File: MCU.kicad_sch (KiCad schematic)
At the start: 22 parts, among them J10 TIM3_OUT_CONN, J11 Conn_01x05_Pin, J12 Conn_01x04_Pin, J13 GPIO_OUT_CONN, J8 Conn_01x08_Pin, Y1 ABM3-8.000MHZ-D2Y-T

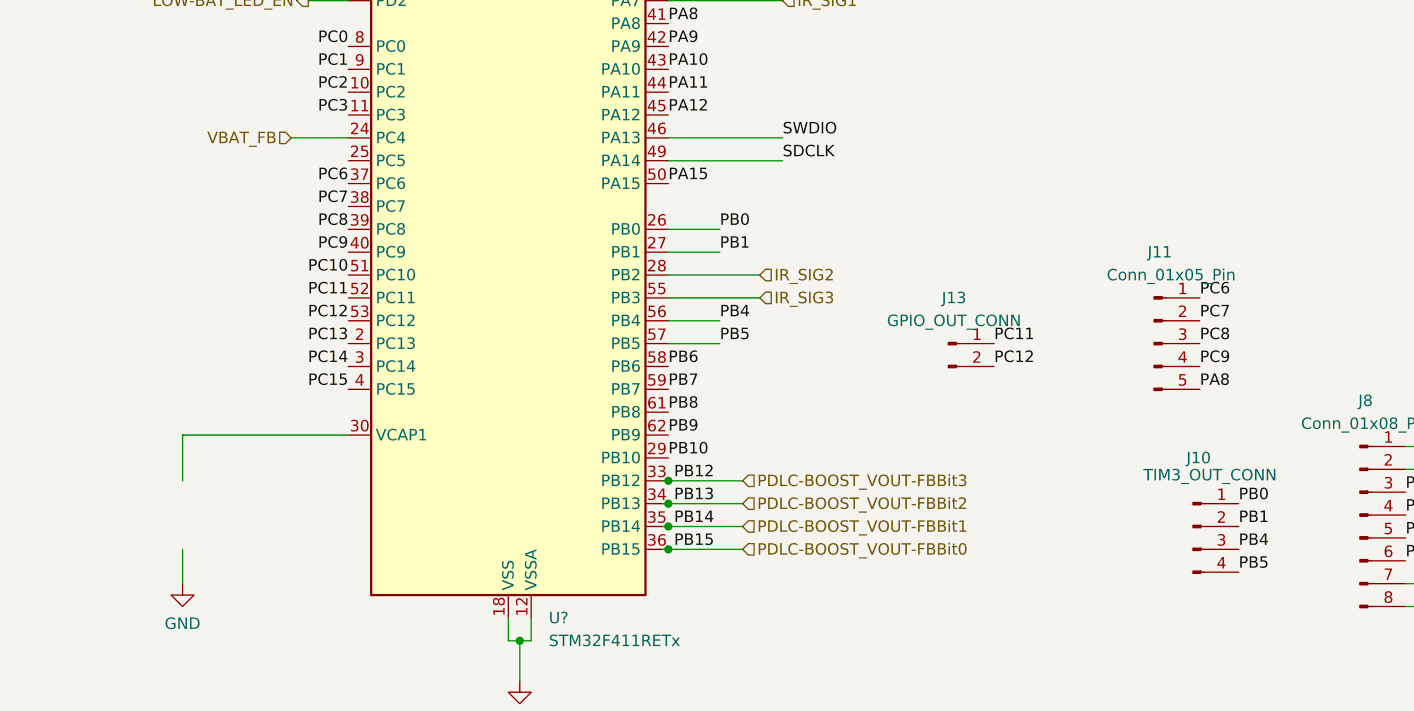
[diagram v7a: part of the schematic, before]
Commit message: PCBv2.02
Toepassingen van wouters feedback.
Condensatoren beter geplaatst bij pdlc, mosfet toegevoegd bij fb bat, extra vias toegevoegd en traces verschoven voor betere GND plane connecties
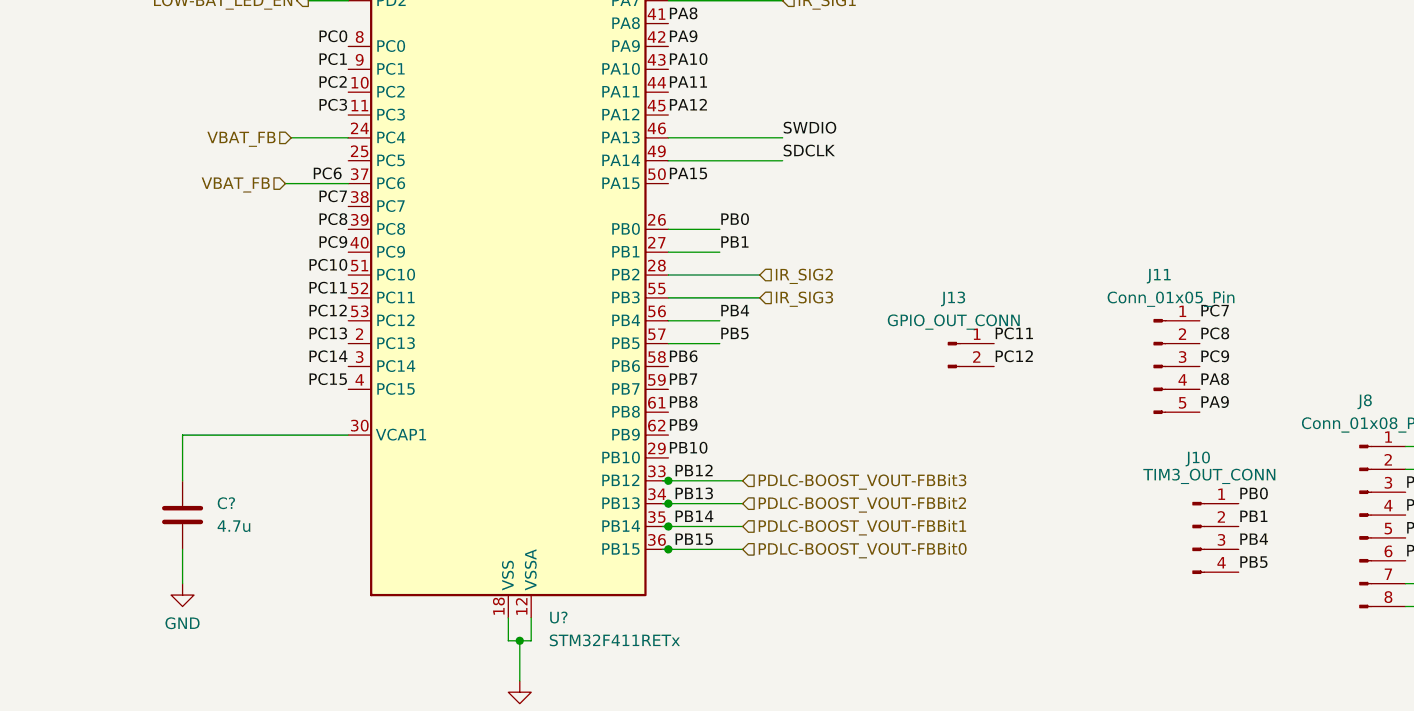
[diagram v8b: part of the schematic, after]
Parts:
- added C?: 4.7u, Capacitor_SMD:C_0805_2012Metric_Pad1.18x1.45mm_HandSolder, symbol Device:C
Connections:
- net GND: now also C?.2
- net PA8: now also J11.4 (Pin_4); no longer J11.5 (Pin_5)
- net PA9: now also J11.5 (Pin_5)
- net PC7: now also J11.1 (Pin_1); no longer J11.2 (Pin_2)
- net PC8: now also J11.2 (Pin_2); no longer J11.3 (Pin_3)
- net PC9: now also J11.3 (Pin_3); no longer J11.4 (Pin_4)
- net VBAT_FB: now also U?.37 (PC6)
- net at U?.30 (VCAP1): now also C?.1
- removed net PC6: J11.1 (Pin_1), U?.37 (PC6)
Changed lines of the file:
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@@
+    (stroke (width 0) (type default))
+  )
+  (wire (pts (xy 119.38 93.98) (xy 126.365 93.98))
     (stroke (width 0) (type default))
   )
@@
     (effects (font (size 1.27 1.27)) (justify left bottom))
   )
-  (label "PC6" (at 220.98 106.68 0) (fields_autoplaced)
-    (effects (font (size 1.27 1.27)) (justify left bottom))
-  )
   (label "PB0" (at 167.64 99.06 0) (fields_autoplaced)
     (effects (font (size 1.27 1.27)) (justify left bottom))
@@
     (effects (font (size 1.27 1.27)) (justify left bottom))
   )
-  (label "PC6" (at 126.365 93.98 180) (fields_autoplaced)
+  (label "PC6" (at 125.73 93.98 180) (fields_autoplaced)
     (effects (font (size 1.27 1.27)) (justify right bottom))
   )
@@
   )
   (label "PB13" (at 162.56 129.54 0) (fields_autoplaced)
+    (effects (font (size 1.27 1.27)) (justify left bottom))
+  )
+  (label "PA9" (at 220.98 119.38 0) (fields_autoplaced)
     (effects (font (size 1.27 1.27)) (justify left bottom))
   )
@@
   (hierarchical_label "H-BRIDGE_IN_B" (shape output) (at 174.752 58.42 0) (fields_autoplaced)
     (effects (font (size 1.27 1.27)) (justify left))
+  )
+  (hierarchical_label "VBAT_FB" (shape input) (at 119.38 93.98 180) (fields_autoplaced)
+    (effects (font (size 1.27 1.27)) (justify right))
   )
   (symbol (lib_id "power:GND") (at 251.46 125.73 0) (unit 1)
@@
     )
   )
+  (symbol (lib_id "Device:C") (at 107.95 130.81 0) (unit 1)
+    (in_bom yes) (on_board yes) (dnp no) (fields_autoplaced)
+    (property "Reference" "C?" (at 111.76 129.54 0)
+      (effects (font (size 1.27 1.27)) (justify left))
+    )
+    (property "Value" "4.7u" (at 111.76 132.08 0)
+      (effects (font (size 1.27 1.27)) (justify left))
+    )
+    (property "Footprint" "Capacitor_SMD:C_0805_2012Metric_Pad1.18x1.45mm_HandSolder" (at 108.9152 134.62 0)
+      (effects (font (size 1.27 1.27)) hide)
+    )
+    (property "Datasheet" "~" (at 107.95 130.81 0)
+      (effects (font (size 1.27 1.27)) hide)
+    )
+    (pin "1")
+    (pin "2")
+    (instances
+      (project "RookBril"
+        (path "/5dc439a9-720d-4bdc-b61f-78a76fde4df5"
+          (reference "C?") (unit 1)
+        )
+        (path "/5dc439a9-720d-4bdc-b61f-78a76fde4df5/d4272076-6289-417e-a51e-9430beab01b7"
+          (reference "C29") (unit 1)
+        )
+      )
+    )
+  )
   (symbol (lib_id "Connector:Conn_01x03_Pin") (at 27.94 60.96 0) (unit 1)
     (in_bom yes) (on_board yes) (dnp no)
@@
     )
   )
-  (symbol (lib_id "power:+3V0") (at 251.46 138.43 0) (unit 1)
-    (in_bom yes) (on_board yes) (dnp no) (fields_autoplaced)
-    (property "Reference" "#PWR?" (at 251.46 142.24 0)
-      (effects (font (size 1.27 1.27)) hide)
-    )
-    (property "Value" "+3V0" (at 251.46 134.62 0)
-      (effects (font (size 1.27 1.27)))
-    )
-    (property "Footprint" "" (at 251.46 138.43 0)
-      (effects (font (size 1.27 1.27)) hide)
-    )
-    (property "Datasheet" "" (at 251.46 138.43 0)
-      (effects (font (size 1.27 1.27)) hide)
-    )
-    (pin "1")
-    (instances
-      (project "RookBril"
-        (path "/5dc439a9-720d-4bdc-b61f-78a76fde4df5"
-          (reference "#PWR?") (unit 1)
-        )
-        (path "/5dc439a9-720d-4bdc-b61f-78a76fde4df5/d4272076-6289-417e-a51e-9430beab01b7"
-          (reference "#PWR070") (unit 1)
-        )
-      )
-    )
-  )
-  (symbol (lib_id "power:+3V0") (at 98.425 17.78 0) (unit 1)
-    (in_bom yes) (on_board yes) (dnp no) (fields_autoplaced)
-    (property "Reference" "#PWR?" (at 98.425 21.59 0)
-      (effects (font (size 1.27 1.27)) hide)
-    )
-    (property "Value" "+3V0" (at 98.425 13.97 0)
-      (effects (font (size 1.27 1.27)))
-    )
-    (property "Footprint" "" (at 98.425 17.78 0)
-      (effects (font (size 1.27 1.27)) hide)
-    )
-    (property "Datasheet" "" (at 98.425 17.78 0)
-      (effects (font (size 1.27 1.27)) hide)
-    )
-    (pin "1")
-    (instances
-      (project "RookBril"
-        (path "/5dc439a9-720d-4bdc-b61f-78a76fde4df5"
-          (reference "#PWR?") (unit 1)
-        )
-        (path "/5dc439a9-720d-4bdc-b61f-78a76fde4df5/d4272076-6289-417e-a51e-9430beab01b7"
-          (reference "#PWR030") (unit 1)
-        )
-      )
-    )
-  )
-  (symbol (lib_id "Connector:Conn_01x05_Pin") (at 215.9 111.76 0) (unit 1)
+  (symbol (lib_id "Connector:Conn_01x05_Pin") (at 215.9 114.3 0) (unit 1)
     (in_bom yes) (on_board yes) (dnp no)
-    (property "Reference" "J11" (at 216.535 101.6 0)
-      (effects (font (size 1.27 1.27)))
-    )
-    (property "Value" "Conn_01x05_Pin" (at 217.805 104.14 0)
-      (effects (font (size 1.27 1.27)))
-    )
-    (property "Footprint" "Connector_PinHeader_2.54mm:PinHeader_1x05_P2.54mm_Vertical" (at 215.9 111.76 0)
-      (effects (font (size 1.27 1.27)) hide)
-    )
-    (property "Datasheet" "~" (at 215.9 111.76 0)
+    (property "Reference" "J11" (at 216.535 104.14 0)
+      (effects (font (size 1.27 1.27)))
+    )
+    (property "Value" "Conn_01x05_Pin" (at 217.805 106.68 0)
+      (effects (font (size 1.27 1.27)))
+    )
+    (property "Footprint" "Connector_PinHeader_2.54mm:PinHeader_1x05_P2.54mm_Vertical" (at 215.9 114.3 0)
+      (effects (font (size 1.27 1.27)) hide)
+    )
+    (property "Datasheet" "~" (at 215.9 114.3 0)
       (effects (font (size 1.27 1.27)) hide)
     )
@@
         )
       )
+    )
+  )
+  (symbol (lib_id "power:+3V0") (at 251.46 138.43 0) (unit 1)
+    (in_bom yes) (on_board yes) (dnp no) (fields_autoplaced)
+    (property "Reference" "#PWR?" (at 251.46 142.24 0)
+      (effects (font (size 1.27 1.27)) hide)
+    )
+    (property "Value" "+3V0" (at 251.46 134.62 0)
+      (effects (font (size 1.27 1.27)))
+    )
+    (property "Footprint" "" (at 251.46 138.43 0)
+      (effects (font (size 1.27 1.27)) hide)
+    )
+    (property "Datasheet" "" (at 251.46 138.43 0)
+      (effects (font (size 1.27 1.27)) hide)
+    )
+    (pin "1")
+    (instances
+      (project "RookBril"
+        (path "/5dc439a9-720d-4bdc-b61f-78a76fde4df5"
+          (reference "#PWR?") (unit 1)
+        )
+        (path "/5dc439a9-720d-4bdc-b61f-78a76fde4df5/d4272076-6289-417e-a51e-9430beab01b7"
+          (reference "#PWR070") (unit 1)
+        )
+      )
+    )
+  )
+  (symbol (lib_id "power:+3V0") (at 98.425 17.78 0) (unit 1)
+    (in_bom yes) (on_board yes) (dnp no) (fields_autoplaced)
+    (property "Reference" "#PWR?" (at 98.425 21.59 0)
+      (effects (font (size 1.27 1.27)) hide)
+    )
+    (property "Value" "+3V0" (at 98.425 13.97 0)
+      (effects (font (size 1.27 1.27)))
+    )
+    (property "Footprint" "" (at 98.425 17.78 0)
+      (effects (font (size 1.27 1.27)) hide)
+    )
+    (property "Datasheet" "" (at 98.425 17.78 0)
+      (effects (font (size 1.27 1.27)) hide)
+    )
+    (pin "1")
+    (instances
+      (project "RookBril"
+        (path "/5dc439a9-720d-4bdc-b61f-78a76fde4df5"
+          (reference "#PWR?") (unit 1)
+        )
+        (path "/5dc439a9-720d-4bdc-b61f-78a76fde4df5/d4272076-6289-417e-a51e-9430beab01b7"
+          (reference "#PWR030") (unit 1)
+        )
+      )
